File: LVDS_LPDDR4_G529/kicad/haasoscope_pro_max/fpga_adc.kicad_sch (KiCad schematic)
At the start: 2 parts, among them IC1 ADC12DL500ACF_Aligned, U3 Ti90G529_Functions

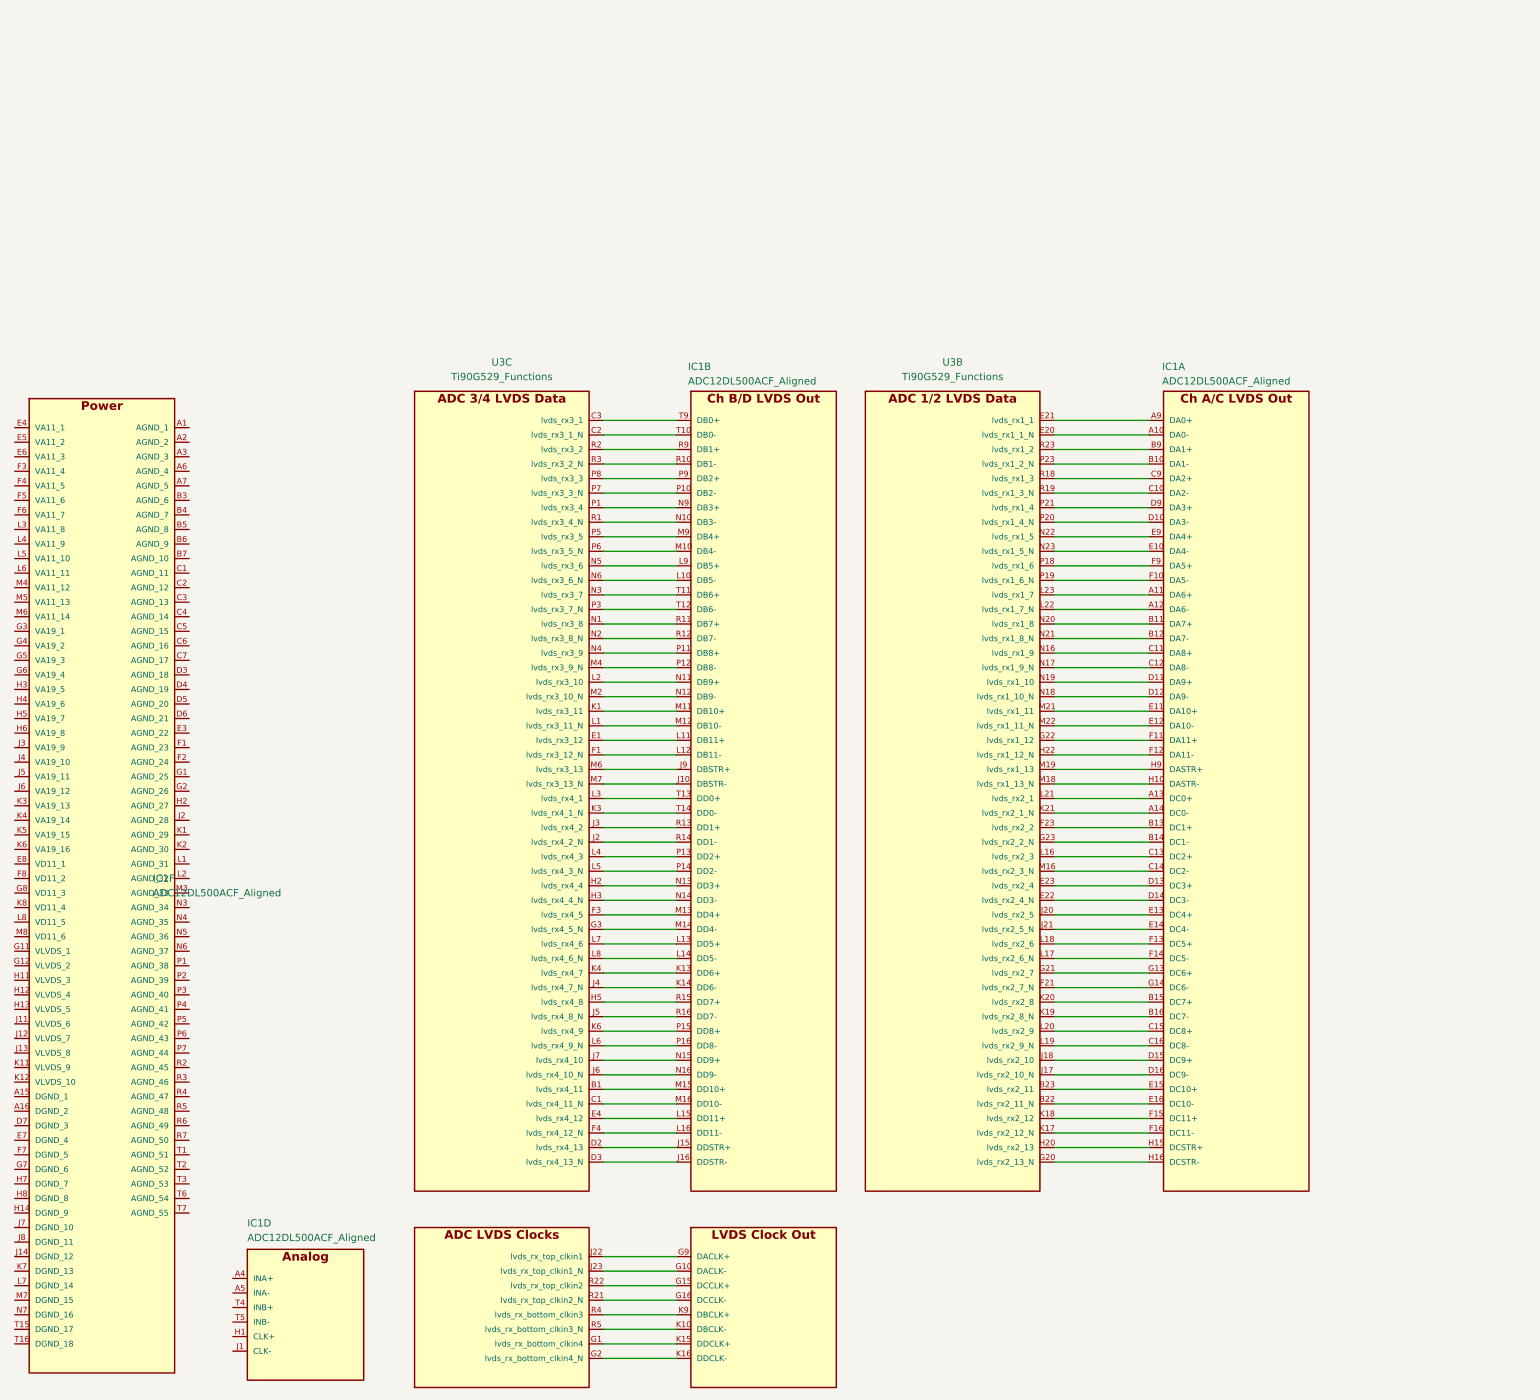
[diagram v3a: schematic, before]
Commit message: Aligned schematics, connected some components
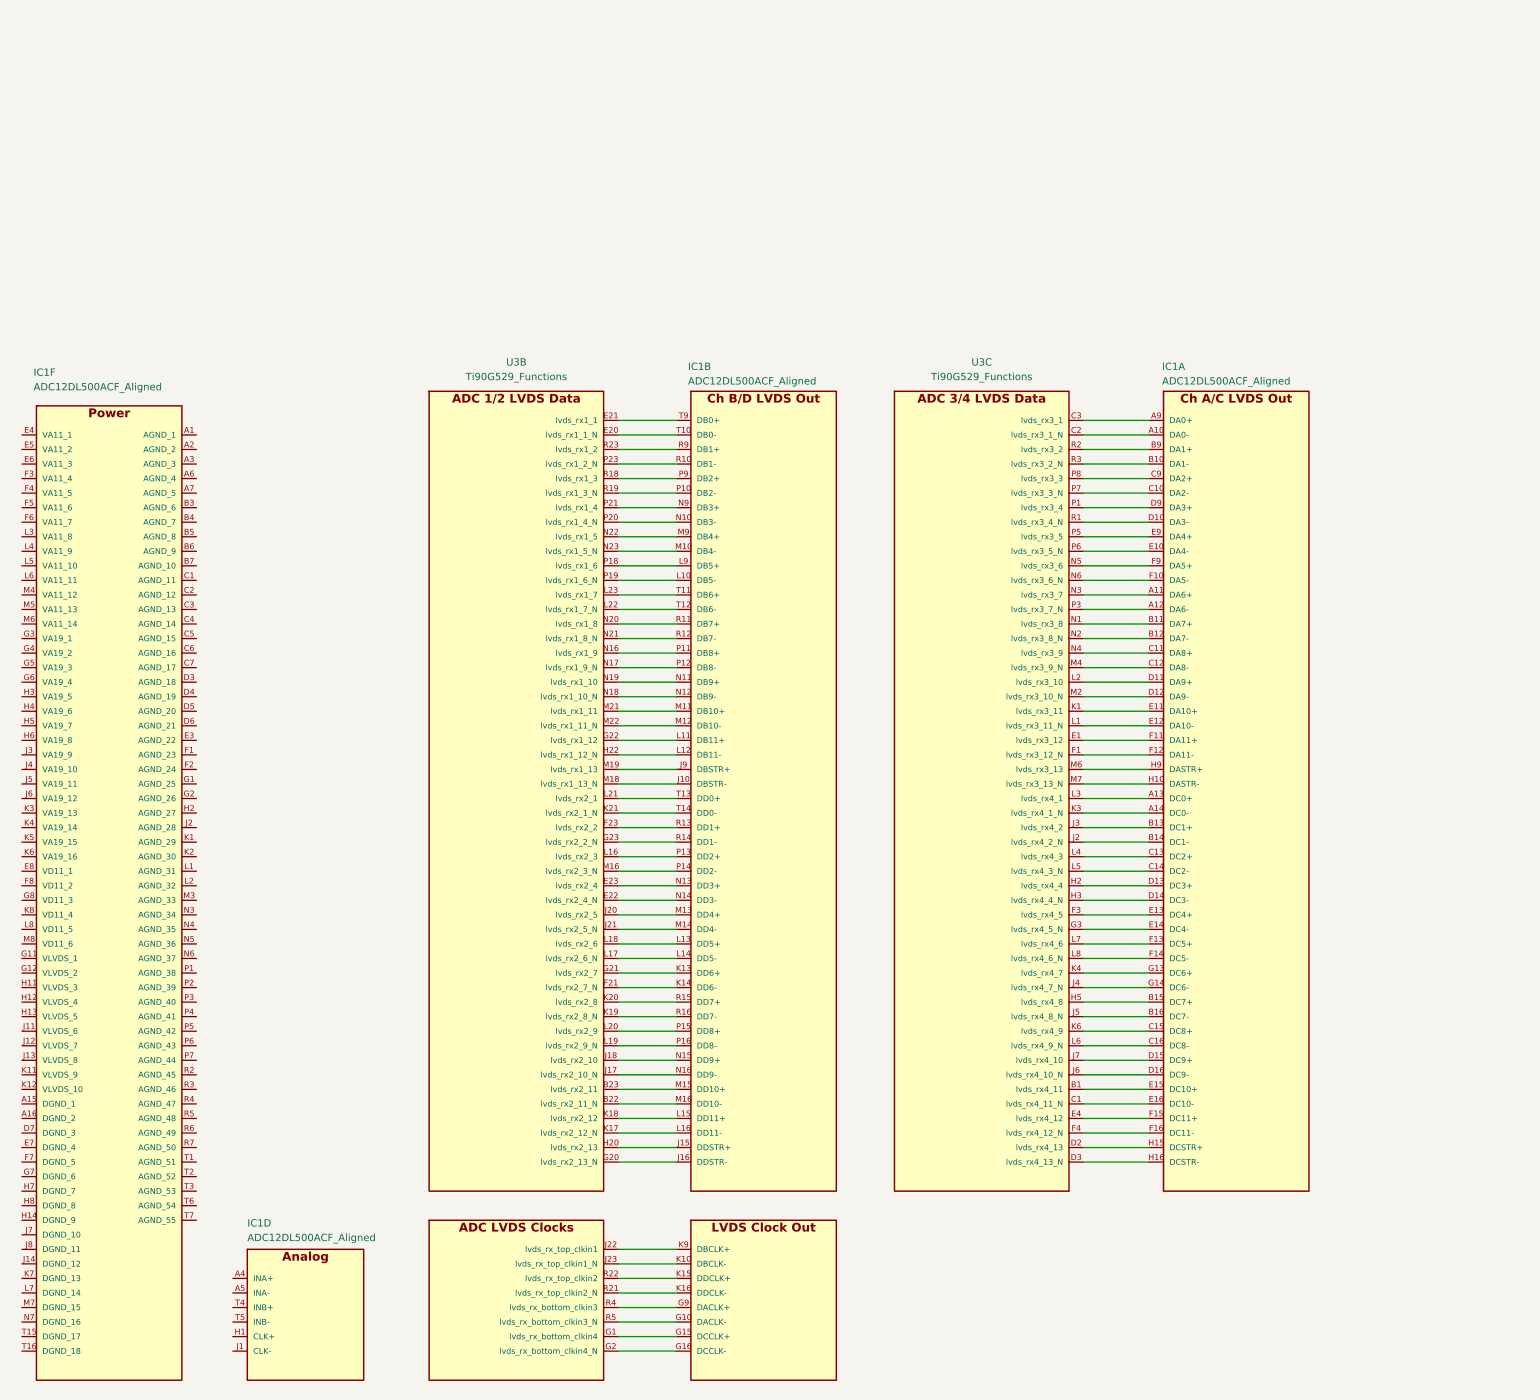
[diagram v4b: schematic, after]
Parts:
- IC1: footprint BGA256C100P16X16_1700X1700X331 -> ADC12DL:BGA256C100P16X16_1700X1700X331
- U3: footprint haasoscope_pro_adc_fpga_board:BGA-529_23x23_19.0x19.0mm -> G529:BGA-529_23x23_19.0x19.0mm
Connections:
- net at U3.B1 (lvds_rx4_11): now also IC1.E15 (DC10+); no longer IC1.M15 (DD10+)
- net at U3.C1 (lvds_rx4_11_N): now also IC1.E16 (DC10-); no longer IC1.M16 (DD10-)
- net at U3.C2 (lvds_rx3_1_N): now also IC1.A10 (DA0-); no longer IC1.T10 (DB0-)
- net at U3.C3 (lvds_rx3_1): now also IC1.A9 (DA0+); no longer IC1.T9 (DB0+)
- net at U3.D2 (lvds_rx4_13): now also IC1.H15 (DCSTR+); no longer IC1.J15 (DDSTR+)
- net at U3.D3 (lvds_rx4_13_N): now also IC1.H16 (DCSTR-); no longer IC1.J16 (DDSTR-)
- net at U3.E1 (lvds_rx3_12): now also IC1.F11 (DA11+); no longer IC1.L11 (DB11+)
- net at U3.E4 (lvds_rx4_12): now also IC1.F15 (DC11+); no longer IC1.L15 (DD11+)
- net at U3.F1 (lvds_rx3_12_N): now also IC1.F12 (DA11-); no longer IC1.L12 (DB11-)
- net at U3.F3 (lvds_rx4_5): now also IC1.E13 (DC4+); no longer IC1.M13 (DD4+)
- net at U3.F4 (lvds_rx4_12_N): now also IC1.F16 (DC11-); no longer IC1.L16 (DD11-)
- net at U3.G3 (lvds_rx4_5_N): now also IC1.E14 (DC4-); no longer IC1.M14 (DD4-)
- net at U3.H2 (lvds_rx4_4): now also IC1.D13 (DC3+); no longer IC1.N13 (DD3+)
- net at U3.H3 (lvds_rx4_4_N): now also IC1.D14 (DC3-); no longer IC1.N14 (DD3-)
- net at U3.H5 (lvds_rx4_8): now also IC1.B15 (DC7+); no longer IC1.R15 (DD7+)
- net at U3.J2 (lvds_rx4_2_N): now also IC1.B14 (DC1-); no longer IC1.R14 (DD1-)
- net at U3.J3 (lvds_rx4_2): now also IC1.B13 (DC1+); no longer IC1.R13 (DD1+)
- net at U3.J4 (lvds_rx4_7_N): now also IC1.G14 (DC6-); no longer IC1.K14 (DD6-)
- net at U3.J5 (lvds_rx4_8_N): now also IC1.B16 (DC7-); no longer IC1.R16 (DD7-)
- net at U3.J6 (lvds_rx4_10_N): now also IC1.D16 (DC9-); no longer IC1.N16 (DD9-)
- net at U3.J7 (lvds_rx4_10): now also IC1.D15 (DC9+); no longer IC1.N15 (DD9+)
- net at U3.K1 (lvds_rx3_11): now also IC1.E11 (DA10+); no longer IC1.M11 (DB10+)
- net at U3.K3 (lvds_rx4_1_N): now also IC1.A14 (DC0-); no longer IC1.T14 (DD0-)
- net at U3.K4 (lvds_rx4_7): now also IC1.G13 (DC6+); no longer IC1.K13 (DD6+)
- net at U3.K6 (lvds_rx4_9): now also IC1.C15 (DC8+); no longer IC1.P15 (DD8+)
- net at U3.L1 (lvds_rx3_11_N): now also IC1.E12 (DA10-); no longer IC1.M12 (DB10-)
- net at U3.L2 (lvds_rx3_10): now also IC1.D11 (DA9+); no longer IC1.N11 (DB9+)
- net at U3.L3 (lvds_rx4_1): now also IC1.A13 (DC0+); no longer IC1.T13 (DD0+)
- net at U3.L4 (lvds_rx4_3): now also IC1.C13 (DC2+); no longer IC1.P13 (DD2+)
- net at U3.L5 (lvds_rx4_3_N): now also IC1.C14 (DC2-); no longer IC1.P14 (DD2-)
- net at U3.L6 (lvds_rx4_9_N): now also IC1.C16 (DC8-); no longer IC1.P16 (DD8-)
- net at U3.L7 (lvds_rx4_6): now also IC1.F13 (DC5+); no longer IC1.L13 (DD5+)
- net at U3.L8 (lvds_rx4_6_N): now also IC1.F14 (DC5-); no longer IC1.L14 (DD5-)
- net at U3.M2 (lvds_rx3_10_N): now also IC1.D12 (DA9-); no longer IC1.N12 (DB9-)
- net at U3.M4 (lvds_rx3_9_N): now also IC1.C12 (DA8-); no longer IC1.P12 (DB8-)
- net at U3.M6 (lvds_rx3_13): now also IC1.H9 (DASTR+); no longer IC1.J9 (DBSTR+)
- net at U3.M7 (lvds_rx3_13_N): now also IC1.H10 (DASTR-); no longer IC1.J10 (DBSTR-)
- net at U3.N1 (lvds_rx3_8): now also IC1.B11 (DA7+); no longer IC1.R11 (DB7+)
- net at U3.N2 (lvds_rx3_8_N): now also IC1.B12 (DA7-); no longer IC1.R12 (DB7-)
- net at U3.N3 (lvds_rx3_7): now also IC1.A11 (DA6+); no longer IC1.T11 (DB6+)
- net at U3.N4 (lvds_rx3_9): now also IC1.C11 (DA8+); no longer IC1.P11 (DB8+)
- net at U3.N5 (lvds_rx3_6): now also IC1.F9 (DA5+); no longer IC1.L9 (DB5+)
- net at U3.N6 (lvds_rx3_6_N): now also IC1.F10 (DA5-); no longer IC1.L10 (DB5-)
- net at U3.P1 (lvds_rx3_4): now also IC1.D9 (DA3+); no longer IC1.N9 (DB3+)
- net at U3.P3 (lvds_rx3_7_N): now also IC1.A12 (DA6-); no longer IC1.T12 (DB6-)
- net at U3.P5 (lvds_rx3_5): now also IC1.E9 (DA4+); no longer IC1.M9 (DB4+)
- net at U3.P6 (lvds_rx3_5_N): now also IC1.E10 (DA4-); no longer IC1.M10 (DB4-)
- net at U3.P7 (lvds_rx3_3_N): now also IC1.C10 (DA2-); no longer IC1.P10 (DB2-)
- net at U3.P8 (lvds_rx3_3): now also IC1.C9 (DA2+); no longer IC1.P9 (DB2+)
- net at U3.R1 (lvds_rx3_4_N): now also IC1.D10 (DA3-); no longer IC1.N10 (DB3-)
- net at U3.R2 (lvds_rx3_2): now also IC1.B9 (DA1+); no longer IC1.R9 (DB1+)
- net at U3.R3 (lvds_rx3_2_N): now also IC1.B10 (DA1-); no longer IC1.R10 (DB1-)
- net at U3.B22 (lvds_rx2_11_N): now also IC1.M16 (DD10-); no longer IC1.E16 (DC10-)
- net at U3.B23 (lvds_rx2_11): now also IC1.M15 (DD10+); no longer IC1.E15 (DC10+)
- net at U3.E20 (lvds_rx1_1_N): now also IC1.T10 (DB0-); no longer IC1.A10 (DA0-)
- net at U3.E21 (lvds_rx1_1): now also IC1.T9 (DB0+); no longer IC1.A9 (DA0+)
- net at U3.E22 (lvds_rx2_4_N): now also IC1.N14 (DD3-); no longer IC1.D14 (DC3-)
- net at U3.E23 (lvds_rx2_4): now also IC1.N13 (DD3+); no longer IC1.D13 (DC3+)
- net at U3.F21 (lvds_rx2_7_N): now also IC1.K14 (DD6-); no longer IC1.G14 (DC6-)
- net at U3.F23 (lvds_rx2_2): now also IC1.R13 (DD1+); no longer IC1.B13 (DC1+)
- net at U3.G20 (lvds_rx2_13_N): now also IC1.J16 (DDSTR-); no longer IC1.H16 (DCSTR-)
- net at U3.G21 (lvds_rx2_7): now also IC1.K13 (DD6+); no longer IC1.G13 (DC6+)
- net at U3.G22 (lvds_rx1_12): now also IC1.L11 (DB11+); no longer IC1.F11 (DA11+)
- net at U3.G23 (lvds_rx2_2_N): now also IC1.R14 (DD1-); no longer IC1.B14 (DC1-)
- net at U3.H20 (lvds_rx2_13): now also IC1.J15 (DDSTR+); no longer IC1.H15 (DCSTR+)
- net at U3.H22 (lvds_rx1_12_N): now also IC1.L12 (DB11-); no longer IC1.F12 (DA11-)
- net at U3.J17 (lvds_rx2_10_N): now also IC1.N16 (DD9-); no longer IC1.D16 (DC9-)
- net at U3.J18 (lvds_rx2_10): now also IC1.N15 (DD9+); no longer IC1.D15 (DC9+)
- net at U3.J20 (lvds_rx2_5): now also IC1.M13 (DD4+); no longer IC1.E13 (DC4+)
- net at U3.J21 (lvds_rx2_5_N): now also IC1.M14 (DD4-); no longer IC1.E14 (DC4-)
- net at U3.K17 (lvds_rx2_12_N): now also IC1.L16 (DD11-); no longer IC1.F16 (DC11-)
- net at U3.K18 (lvds_rx2_12): now also IC1.L15 (DD11+); no longer IC1.F15 (DC11+)
- net at U3.K19 (lvds_rx2_8_N): now also IC1.R16 (DD7-); no longer IC1.B16 (DC7-)
- net at U3.K20 (lvds_rx2_8): now also IC1.R15 (DD7+); no longer IC1.B15 (DC7+)
- net at U3.K21 (lvds_rx2_1_N): now also IC1.T14 (DD0-); no longer IC1.A14 (DC0-)
- net at U3.L16 (lvds_rx2_3): now also IC1.P13 (DD2+); no longer IC1.C13 (DC2+)
- net at U3.L17 (lvds_rx2_6_N): now also IC1.L14 (DD5-); no longer IC1.F14 (DC5-)
- net at U3.L18 (lvds_rx2_6): now also IC1.L13 (DD5+); no longer IC1.F13 (DC5+)
- net at U3.L19 (lvds_rx2_9_N): now also IC1.P16 (DD8-); no longer IC1.C16 (DC8-)
- net at U3.L20 (lvds_rx2_9): now also IC1.P15 (DD8+); no longer IC1.C15 (DC8+)
- net at U3.L21 (lvds_rx2_1): now also IC1.T13 (DD0+); no longer IC1.A13 (DC0+)
- net at U3.L22 (lvds_rx1_7_N): now also IC1.T12 (DB6-); no longer IC1.A12 (DA6-)
- net at U3.L23 (lvds_rx1_7): now also IC1.T11 (DB6+); no longer IC1.A11 (DA6+)
- net at U3.M16 (lvds_rx2_3_N): now also IC1.P14 (DD2-); no longer IC1.C14 (DC2-)
- net at U3.M18 (lvds_rx1_13_N): now also IC1.J10 (DBSTR-); no longer IC1.H10 (DASTR-)
- net at U3.M19 (lvds_rx1_13): now also IC1.J9 (DBSTR+); no longer IC1.H9 (DASTR+)
- net at U3.M21 (lvds_rx1_11): now also IC1.M11 (DB10+); no longer IC1.E11 (DA10+)
- net at U3.M22 (lvds_rx1_11_N): now also IC1.M12 (DB10-); no longer IC1.E12 (DA10-)
- net at U3.N16 (lvds_rx1_9): now also IC1.P11 (DB8+); no longer IC1.C11 (DA8+)
- net at U3.N17 (lvds_rx1_9_N): now also IC1.P12 (DB8-); no longer IC1.C12 (DA8-)
- net at U3.N18 (lvds_rx1_10_N): now also IC1.N12 (DB9-); no longer IC1.D12 (DA9-)
- net at U3.N19 (lvds_rx1_10): now also IC1.N11 (DB9+); no longer IC1.D11 (DA9+)
- net at U3.N20 (lvds_rx1_8): now also IC1.R11 (DB7+); no longer IC1.B11 (DA7+)
- net at U3.N21 (lvds_rx1_8_N): now also IC1.R12 (DB7-); no longer IC1.B12 (DA7-)
- net at U3.N22 (lvds_rx1_5): now also IC1.M9 (DB4+); no longer IC1.E9 (DA4+)
- net at U3.N23 (lvds_rx1_5_N): now also IC1.M10 (DB4-); no longer IC1.E10 (DA4-)
- net at U3.P18 (lvds_rx1_6): now also IC1.L9 (DB5+); no longer IC1.F9 (DA5+)
- net at U3.P19 (lvds_rx1_6_N): now also IC1.L10 (DB5-); no longer IC1.F10 (DA5-)
- net at U3.P20 (lvds_rx1_4_N): now also IC1.N10 (DB3-); no longer IC1.D10 (DA3-)
- net at U3.P21 (lvds_rx1_4): now also IC1.N9 (DB3+); no longer IC1.D9 (DA3+)
- net at U3.P23 (lvds_rx1_2_N): now also IC1.R10 (DB1-); no longer IC1.B10 (DA1-)
- net at U3.R18 (lvds_rx1_3): now also IC1.P9 (DB2+); no longer IC1.C9 (DA2+)
- net at U3.R19 (lvds_rx1_3_N): now also IC1.P10 (DB2-); no longer IC1.C10 (DA2-)
- net at U3.R23 (lvds_rx1_2): now also IC1.R9 (DB1+); no longer IC1.B9 (DA1+)
- net at U3.G1 (lvds_rx_bottom_clkin4): now also IC1.G15 (DCCLK+); no longer IC1.K15 (DDCLK+)
- net at U3.G2 (lvds_rx_bottom_clkin4_N): now also IC1.G16 (DCCLK-); no longer IC1.K16 (DDCLK-)
- net at U3.J22 (lvds_rx_top_clkin1): now also IC1.K9 (DBCLK+); no longer IC1.G9 (DACLK+)
- net at U3.J23 (lvds_rx_top_clkin1_N): now also IC1.K10 (DBCLK-); no longer IC1.G10 (DACLK-)
- net at U3.R21 (lvds_rx_top_clkin2_N): now also IC1.K16 (DDCLK-); no longer IC1.G16 (DCCLK-)
- net at U3.R22 (lvds_rx_top_clkin2): now also IC1.K15 (DDCLK+); no longer IC1.G15 (DCCLK+)
- net at U3.R4 (lvds_rx_bottom_clkin3): now also IC1.G9 (DACLK+); no longer IC1.K9 (DBCLK+)
- net at U3.R5 (lvds_rx_bottom_clkin3_N): now also IC1.G10 (DACLK-); no longer IC1.K10 (DBCLK-)
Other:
- moved on the sheet: IC1F, U3B, U3C

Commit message: an lvds routed
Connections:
- net lvds_rx1_1_N: now reaches IC1.T10 (DB0-), U3.E20 (lvds_rx1_1_N)
- net lvds_rx1_1_P: now reaches IC1.T9 (DB0+), U3.E21 (lvds_rx1_1)
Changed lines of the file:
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@@
+	(wire
+		(pts
+			(xy 123.19 27.94) (xy 133.35 27.94)
+		)
+		(stroke
+			(width 0)
+			(type default)
+		)
+	)
 	(wire
 		(pts
@@
 	(wire
 		(pts
-			(xy 123.19 27.94) (xy 133.35 27.94)
-		)
-		(stroke
-			(width 0)
-			(type default)
-		)
-	)
-	(wire
-		(pts
 			(xy 123.19 124.46) (xy 133.35 124.46)
 		)
@@
 		)
 	)
+	(label "lvds_rx1_1_N"
+		(at 123.19 27.94 0)
+		(effects
+			(font
+				(size 1.27 1.27)
+			)
+			(justify left bottom)
+		)
+	)
+	(label "lvds_rx1_1_P"
+		(at 123.19 25.4 0)
+		(effects
+			(font
+				(size 1.27 1.27)
+			)
+			(justify left bottom)
+		)
+	)
